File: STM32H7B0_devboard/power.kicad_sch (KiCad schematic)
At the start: 14 parts, among them Q4 AO3401A

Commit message: Breakout
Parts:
- C18: renamed from C26; footprint (none) -> NFM18PC104R1C3D:NFM18PC104R1C3D_MUR
- D3: renamed from D5; value 9v1 -> 10v; footprint (none) -> Diode_SMD:D_SOD-523
- renumbered C27 to C19, C28 to C20, C22 to C21, C29 to C22, C30 to C23, F3 to F1, L4 to L2, Q4 to Q2, R36 to R19, R34 to R20, R35 to R21, U7 to U4
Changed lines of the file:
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@@
 		(on_board yes)
 		(dnp no)
-		(property "Reference" "#PWR060"
+		(property "Reference" "#PWR043"
 			(at 93.98 95.25 0)
 			(effects
@@
 			(project "STM32H7B0_devboard"
 				(path "/0c02ba0f-c40f-484f-a270-dfb4a249f2e6/f5149cbb-8fa8-437a-8f6e-43d0a2b09eff"
-					(reference "#PWR060")
+					(reference "#PWR043")
 					(unit 1)
 				)
@@
 		(on_board yes)
 		(dnp no)
-		(property "Reference" "U7"
+		(property "Reference" "U4"
 			(at 115.57 26.67 0)
 			(effects
@@
 			)
 		)
-		(property "Datasheet" ""
+		(property "Datasheet" "https://www.lcsc.com/datasheet/lcsc_datasheet_2304241919_Texas-Instruments-TPS563201DDCR_C116592.pdf"
 			(at 110.49 33.02 0)
 			(effects
@@
 			(project "STM32H7B0_devboard"
 				(path "/0c02ba0f-c40f-484f-a270-dfb4a249f2e6/f5149cbb-8fa8-437a-8f6e-43d0a2b09eff"
-					(reference "U7")
+					(reference "U4")
 					(unit 1)
 				)
@@
 		(on_board yes)
 		(dnp no)
-		(property "Reference" "C28"
+		(property "Reference" "C20"
 			(at 87.122 32.512 0)
 			(effects
@@
 			(project "STM32H7B0_devboard"
 				(path "/0c02ba0f-c40f-484f-a270-dfb4a249f2e6/f5149cbb-8fa8-437a-8f6e-43d0a2b09eff"
-					(reference "C28")
+					(reference "C20")
 					(unit 1)
 				)
@@
 		(on_board yes)
 		(dnp no)
-		(property "Reference" "C29"
+		(property "Reference" "C22"
 			(at 71.882 80.772 0)
 			(effects
@@
 			(project "STM32H7B0_devboard"
 				(path "/0c02ba0f-c40f-484f-a270-dfb4a249f2e6/f5149cbb-8fa8-437a-8f6e-43d0a2b09eff"
-					(reference "C29")
+					(reference "C22")
 					(unit 1)
 				)
@@
 		(on_board yes)
 		(dnp no)
-		(property "Reference" "C27"
+		(property "Reference" "C19"
 			(at 80.772 32.512 0)
 			(effects
@@
 			(project "STM32H7B0_devboard"
 				(path "/0c02ba0f-c40f-484f-a270-dfb4a249f2e6/f5149cbb-8fa8-437a-8f6e-43d0a2b09eff"
-					(reference "C27")
+					(reference "C19")
 					(unit 1)
 				)
@@
 		(on_board yes)
 		(dnp no)
-		(property "Reference" "C26"
+		(property "Reference" "C18"
 			(at 72.39 26.67 0)
 			(effects
@@
 			)
 		)
-		(property "Footprint" ""
+		(property "Footprint" "NFM18PC104R1C3D:NFM18PC104R1C3D_MUR"
 			(at 72.39 31.75 90)
 			(effects
@@
 			)
 		)
-		(property "Datasheet" "~"
+		(property "Datasheet" "https://www.lcsc.com/datasheet/lcsc_datasheet_1811021520_Murata-Electronics-NFM18PC104R1C3D_C111493.pdf"
 			(at 72.39 31.75 90)
 			(effects
@@
 			)
 		)
-		(property "Description" "NFM31KC104R2A3L"
+		(property "Description" "NFM18PC104R1C3D"
 			(at 72.39 23.876 0)
 			(effects
@@
 					(size 1.27 1.27)
 				)
+				(hide yes)
 			)
 		)
@@
 			(project "STM32H7B0_devboard"
 				(path "/0c02ba0f-c40f-484f-a270-dfb4a249f2e6/f5149cbb-8fa8-437a-8f6e-43d0a2b09eff"
-					(reference "C26")
+					(reference "C18")
 					(unit 1)
 				)
@@
 		(on_board yes)
 		(dnp no)
-		(property "Reference" "#PWR062"
+		(property "Reference" "#PWR042"
 			(at 74.93 92.71 0)
 			(effects
@@
 			(project "STM32H7B0_devboard"
 				(path "/0c02ba0f-c40f-484f-a270-dfb4a249f2e6/f5149cbb-8fa8-437a-8f6e-43d0a2b09eff"
-					(reference "#PWR062")
+					(reference "#PWR042")
 					(unit 1)
 				)
@@
 		(on_board yes)
 		(dnp no)
-		(property "Reference" "R36"
+		(property "Reference" "R19"
 			(at 53.34 42.926 90)
 			(effects
@@
 			(project "STM32H7B0_devboard"
 				(path "/0c02ba0f-c40f-484f-a270-dfb4a249f2e6/f5149cbb-8fa8-437a-8f6e-43d0a2b09eff"
-					(reference "R36")
+					(reference "R19")
 					(unit 1)
 				)
@@
 		(on_board yes)
 		(dnp no)
-		(property "Reference" "#PWR061"
+		(property "Reference" "#PWR041"
 			(at 64.77 54.61 0)
 			(effects
@@
 			(project "STM32H7B0_devboard"
 				(path "/0c02ba0f-c40f-484f-a270-dfb4a249f2e6/f5149cbb-8fa8-437a-8f6e-43d0a2b09eff"
-					(reference "#PWR061")
+					(reference "#PWR041")
 					(unit 1)
 				)
@@
 		(on_board yes)
 		(dnp no)
-		(property "Reference" "R35"
+		(property "Reference" "R21"
 			(at 91.694 83.82 90)
 			(effects
@@
 			(project "STM32H7B0_devboard"
 				(path "/0c02ba0f-c40f-484f-a270-dfb4a249f2e6/f5149cbb-8fa8-437a-8f6e-43d0a2b09eff"
-					(reference "R35")
+					(reference "R21")
 					(unit 1)
 				)
@@
 		(on_board yes)
 		(dnp no)
-		(property "Reference" "F3"
+		(property "Reference" "F1"
 			(at 44.45 26.67 90)
 			(effects
@@
 			(project "STM32H7B0_devboard"
 				(path "/0c02ba0f-c40f-484f-a270-dfb4a249f2e6/f5149cbb-8fa8-437a-8f6e-43d0a2b09eff"
-					(reference "F3")
+					(reference "F1")
 					(unit 1)
 				)
@@
 		(on_board yes)
 		(dnp no)
-		(property "Reference" "C22"
+		(property "Reference" "C21"
 			(at 91.948 54.102 90)
 			(effects
@@
 			(project "STM32H7B0_devboard"
 				(path "/0c02ba0f-c40f-484f-a270-dfb4a249f2e6/f5149cbb-8fa8-437a-8f6e-43d0a2b09eff"
-					(reference "C22")
+					(reference "C21")
 					(unit 1)
 				)
@@
 		(on_board yes)
 		(dnp no)
-		(property "Reference" "L4"
+		(property "Reference" "L2"
 			(at 64.77 76.2 90)
 			(effects
@@
 			(project "STM32H7B0_devboard"
 				(path "/0c02ba0f-c40f-484f-a270-dfb4a249f2e6/f5149cbb-8fa8-437a-8f6e-43d0a2b09eff"
-					(reference "L4")
+					(reference "L2")
 					(unit 1)
 				)
@@
 		(on_board yes)
 		(dnp no)
-		(property "Reference" "C30"
+		(property "Reference" "C23"
 			(at 79.502 80.772 0)
 			(effects
@@
 			(project "STM32H7B0_devboard"
 				(path "/0c02ba0f-c40f-484f-a270-dfb4a249f2e6/f5149cbb-8fa8-437a-8f6e-43d0a2b09eff"
-					(reference "C30")
+					(reference "C23")
 					(unit 1)
 				)
@@
 		(on_board yes)
 		(dnp no)
-		(property "Reference" "#FLG07"
+		(property "Reference" "#FLG05"
 			(at 86.36 27.305 0)
 			(effects
@@
 			(project "STM32H7B0_devboard"
 				(path "/0c02ba0f-c40f-484f-a270-dfb4a249f2e6/f5149cbb-8fa8-437a-8f6e-43d0a2b09eff"
-					(reference "#FLG07")
+					(reference "#FLG05")
 					(unit 1)
 				)
@@
 		(on_board yes)
 		(dnp no)
-		(property "Reference" "#PWR051"
+		(property "Reference" "#PWR040"
 			(at 101.6 44.45 0)
 			(effects
@@
 			(project "STM32H7B0_devboard"
 				(path "/0c02ba0f-c40f-484f-a270-dfb4a249f2e6/f5149cbb-8fa8-437a-8f6e-43d0a2b09eff"
-					(reference "#PWR051")
+					(reference "#PWR040")
 					(unit 1)
 				)
@@
 		(on_board yes)
 		(dnp no)
-		(property "Reference" "R34"
+		(property "Reference" "R20"
 			(at 89.154 76.2 90)
 			(effects
@@
 			(project "STM32H7B0_devboard"
 				(path "/0c02ba0f-c40f-484f-a270-dfb4a249f2e6/f5149cbb-8fa8-437a-8f6e-43d0a2b09eff"
-					(reference "R34")
+					(reference "R20")
 					(unit 1)
 				)
@@
 		(on_board yes)
 		(dnp no)
-		(property "Reference" "D5"
+		(property "Reference" "D3"
 			(at 61.214 31.496 0)
 			(effects
@@
 			)
 		)
-		(property "Value" "9v1"
+		(property "Value" "10v"
 			(at 66.04 31.242 0)
 			(effects
@@
 			)
 		)
-		(property "Footprint" ""
+		(property "Footprint" "Diode_SMD:D_SOD-523"
 			(at 63.5 33.02 90)
 			(effects
@@
 			)
 		)
-		(property "Datasheet" "~"
+		(property "Datasheet" "https://www.lcsc.com/datasheet/lcsc_datasheet_2304140030_Nexperia-BZX585-B10-115_C455021.pdf"
 			(at 63.5 33.02 90)
 			(effects
@@
 			)
 		)
-		(property "Description" "BZX585-B9v1"
+		(property "Description" "BZX585-B10"
 			(at 63.5 21.082 90)
 			(effects
@@
 					(size 1.27 1.27)
 				)
-			)
-		)
-		(pin "2"
-		)
-		(pin "1"
-		)
-		(instances
-			(project "STM32H7B0_devboard"
-				(path "/0c02ba0f-c40f-484f-a270-dfb4a249f2e6/f5149cbb-8fa8-437a-8f6e-43d0a2b09eff"
-					(reference "D5")
+				(hide yes)
+			)
+		)
+		(pin "2"
+		)
+		(pin "1"
+		)
+		(instances
+			(project "STM32H7B0_devboard"
+				(path "/0c02ba0f-c40f-484f-a270-dfb4a249f2e6/f5149cbb-8fa8-437a-8f6e-43d0a2b09eff"
+					(reference "D3")
 					(unit 1)
 				)
@@
 		(on_board yes)
 		(dnp no)
-		(property "Reference" "Q4"
+		(property "Reference" "Q2"
 			(at 55.88 25.654 90)
 			(effects
@@
 					(size 1.27 1.27)
 				)
+				(hide yes)
 			)
 		)
@@
 			(project "STM32H7B0_devboard"
 				(path "/0c02ba0f-c40f-484f-a270-dfb4a249f2e6/f5149cbb-8fa8-437a-8f6e-43d0a2b09eff"
-					(reference "Q4")
-					(unit 1)
-				)
+					(reference "Q2")
+					(unit 1)
+				)

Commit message: Schematic V2.0 + Footprints
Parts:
- L2: footprint (none) -> Inductor_SMD:L_0603_1608Metric
- R19, R20, R21: footprint (none) -> Resistor_SMD:R_0402_1005Metric
- U4: footprint (none) -> Package_TO_SOT_SMD:SOT-23-6
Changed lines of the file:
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@@
 			)
 		)
-		(property "Footprint" ""
+		(property "Footprint" "Package_TO_SOT_SMD:SOT-23-6"
 			(at 110.49 33.02 0)
 			(effects
@@
 			)
 		)
-		(property "Footprint" ""
+		(property "Footprint" "Resistor_SMD:R_0402_1005Metric"
 			(at 55.88 43.18 0)
 			(effects
@@
 			)
 		)
-		(property "Footprint" ""
+		(property "Footprint" "Resistor_SMD:R_0402_1005Metric"
 			(at 93.98 83.82 0)
 			(effects
@@
 			)
 		)
-		(property "Footprint" ""
+		(property "Footprint" "Inductor_SMD:L_0603_1608Metric"
 			(at 64.77 78.74 0)
 			(effects
@@
 			)
 		)
-		(property "Description" "Inductor, small symbol"
+		(property "Description" "MPL1608S2R2MHT"
 			(at 64.77 78.74 0)
 			(effects
@@
 			)
 		)
-		(property "Footprint" ""
+		(property "Footprint" "Resistor_SMD:R_0402_1005Metric"
 			(at 88.9 78.74 0)
 			(effects

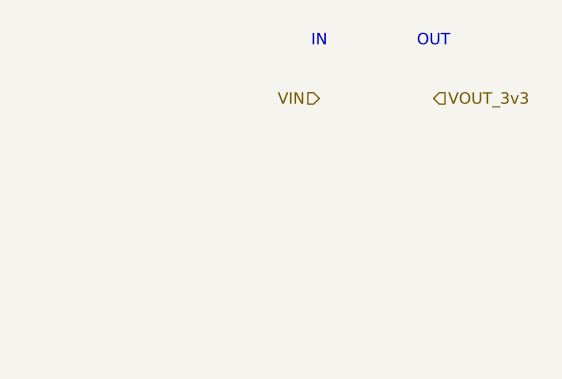
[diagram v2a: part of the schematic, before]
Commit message: Updated .gitignore
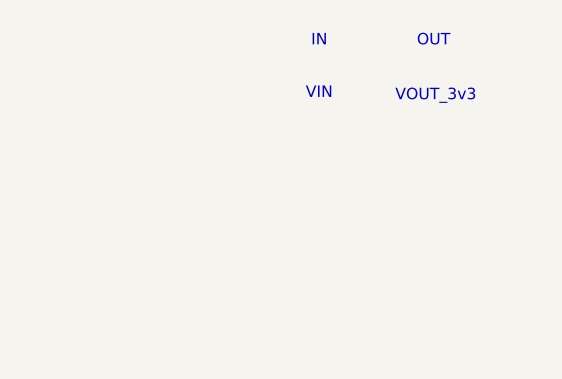
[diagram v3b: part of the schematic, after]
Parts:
- C21: footprint Capacitor_SMD:C_0603_1608Metric -> Capacitor_SMD:C_1206_3216Metric
- L2: footprint Inductor_SMD:L_0603_1608Metric -> Inductor_SMD:L_Changjiang_FNR3015S
- R19, R20, R21: footprint Resistor_SMD:R_0402_1005Metric -> Resistor_SMD:R_0603_1608Metric
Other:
- note added: "VIN"
- note added: "VOUT_3v3"
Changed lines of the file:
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@@
+		)
+	)
+	(text "VOUT_3v3"
+		(exclude_from_sim no)
+		(at 260.604 25.146 0)
+		(effects
+			(font
+				(size 1.27 1.27)
+			)
 		)
 	)
@@
 		(exclude_from_sim no)
 		(at 247.65 19.05 0)
+		(effects
+			(font
+				(size 1.27 1.27)
+			)
+		)
+	)
+	(text "VIN"
+		(exclude_from_sim no)
+		(at 247.65 24.892 0)
 		(effects
 			(font
@@
 		)
 	)
+	(label "BUCK_SW"
+		(at 102.87 34.29 180)
+		(fields_autoplaced yes)
+		(effects
+			(font
+				(size 1.27 1.27)
+			)
+			(justify right bottom)
+		)
+	)
+	(label "BUCK_FB"
+		(at 97.79 80.01 0)
+		(fields_autoplaced yes)
+		(effects
+			(font
+				(size 1.27 1.27)
+			)
+			(justify left bottom)
+		)
+	)
+	(label "BUCK_EN"
+		(at 91.44 29.21 0)
+		(fields_autoplaced yes)
+		(effects
+			(font
+				(size 1.27 1.27)
+			)
+			(justify left bottom)
+		)
+	)
 	(label "BUCK_EN"
 		(at 119.38 34.29 0)
@@
 			(justify left bottom)
 		)
-		(property "Netclass" ""
-			(at 119.38 35.56 0)
-			(effects
-				(font
-					(size 1.27 1.27)
-				)
-				(justify left)
-				(hide yes)
-			)
-		)
-	)
-	(label "BUCK_SW"
-		(at 102.87 34.29 180)
-		(fields_autoplaced yes)
-		(effects
-			(font
-				(size 1.27 1.27)
-			)
-			(justify right bottom)
-		)
-	)
-	(label "BUCK_FB"
-		(at 97.79 80.01 0)
-		(fields_autoplaced yes)
-		(effects
-			(font
-				(size 1.27 1.27)
-			)
-			(justify left bottom)
-		)
-	)
-	(label "BUCK_EN"
-		(at 91.44 29.21 0)
-		(fields_autoplaced yes)
-		(effects
-			(font
-				(size 1.27 1.27)
-			)
-			(justify left bottom)
-		)
 	)
 	(label "BUCK_BST"
@@
 			)
 			(justify left bottom)
-		)
-	)
-	(hierarchical_label "VOUT_3v3"
-		(shape input)
-		(at 260.35 25.4 0)
-		(fields_autoplaced yes)
-		(effects
-			(font
-				(size 1.27 1.27)
-			)
-			(justify left)
 		)
 	)
@@
 		)
 	)
-	(hierarchical_label "VIN"
-		(shape input)
-		(at 247.65 25.4 180)
-		(fields_autoplaced yes)
-		(effects
-			(font
-				(size 1.27 1.27)
-			)
-			(justify right)
-		)
-	)
 	(hierarchical_label "VOUT_3v3"
 		(shape input)
@@
 			)
 		)
-		(property "Footprint" "Resistor_SMD:R_0402_1005Metric"
+		(property "Footprint" "Resistor_SMD:R_0603_1608Metric"
 			(at 55.88 43.18 0)
 			(effects
@@
 			)
 		)
-		(property "Footprint" "Resistor_SMD:R_0402_1005Metric"
+		(property "Footprint" "Resistor_SMD:R_0603_1608Metric"
 			(at 93.98 83.82 0)
 			(effects
@@
 			)
 		)
-		(property "Footprint" "Capacitor_SMD:C_0603_1608Metric"
+		(property "Footprint" "Capacitor_SMD:C_1206_3216Metric"
 			(at 90.17 57.15 0)
 			(effects
@@
 			)
 		)
-		(property "Footprint" "Inductor_SMD:L_0603_1608Metric"
+		(property "Footprint" "Inductor_SMD:L_Changjiang_FNR3015S"
 			(at 64.77 78.74 0)
 			(effects
@@
 			)
 		)
-		(property "Description" "MPL1608S2R2MHT"
+		(property "Description" "FNR3015S2R2MT"
 			(at 64.77 78.74 0)
 			(effects
@@
 			)
 		)
-		(property "Footprint" "Resistor_SMD:R_0402_1005Metric"
+		(property "Footprint" "Resistor_SMD:R_0603_1608Metric"
 			(at 88.9 78.74 0)
 			(effects

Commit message: Done V1
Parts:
- C18: LCSC (none) -> C111493
- C19, C20: LCSC (none) -> C9807
- C21: LCSC (none) -> C110255
- C22, C23: LCSC (none) -> C12891
- D3: LCSC (none) -> C455021
- F1: LCSC (none) -> C2830236
- L2: LCSC (none) -> C167747
- Q2: LCSC (none) -> C347476
- R19, R21: LCSC (none) -> C25804
- R20: LCSC (none) -> C23003
- U4: LCSC (none) -> C116592
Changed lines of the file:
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@@
+			)
+		)
+		(property "LCSC" "C116592"
+			(at 110.49 33.02 0)
+			(effects
+				(font
+					(size 1.27 1.27)
+				)
+				(hide yes)
 			)
 		)
@@
 			)
 		)
+		(property "LCSC" " C9807"
+			(at 86.36 34.29 0)
+			(effects
+				(font
+					(size 1.27 1.27)
+				)
+				(hide yes)
+			)
+		)
 		(pin "2"
 		)
@@
 			)
 		)
+		(property "LCSC" "C12891"
+			(at 71.12 82.55 0)
+			(effects
+				(font
+					(size 1.27 1.27)
+				)
+				(hide yes)
+			)
+		)
 		(pin "2"
 		)
@@
 			)
 		)
+		(property "LCSC" " C9807"
+			(at 80.01 34.29 0)
+			(effects
+				(font
+					(size 1.27 1.27)
+				)
+				(hide yes)
+			)
+		)
 		(pin "2"
 		)
@@
 			)
 		)
+		(property "LCSC" "C111493"
+			(at 72.39 31.75 0)
+			(effects
+				(font
+					(size 1.27 1.27)
+				)
+				(hide yes)
+			)
+		)
 		(pin "1"
 		)
@@
 			)
 		)
+		(property "LCSC" "C25804"
+			(at 55.88 43.18 0)
+			(effects
+				(font
+					(size 1.27 1.27)
+				)
+				(hide yes)
+			)
+		)
 		(pin "1"
 		)
@@
 			)
 		)
+		(property "LCSC" "C25804"
+			(at 93.98 83.82 0)
+			(effects
+				(font
+					(size 1.27 1.27)
+				)
+				(hide yes)
+			)
+		)
 		(pin "1"
 		)
@@
 			)
 		)
+		(property "LCSC" "C2830236"
+			(at 44.45 29.21 0)
+			(effects
+				(font
+					(size 1.27 1.27)
+				)
+				(hide yes)
+			)
+		)
 		(pin "2"
 		)
@@
 			)
 		)
+		(property "LCSC" "C110255"
+			(at 90.17 57.15 0)
+			(effects
+				(font
+					(size 1.27 1.27)
+				)
+				(hide yes)
+			)
+		)
 		(pin "2"
 		)
@@
 			)
 		)
+		(property "LCSC" "C167747"
+			(at 64.77 78.74 0)
+			(effects
+				(font
+					(size 1.27 1.27)
+				)
+				(hide yes)
+			)
+		)
 		(pin "2"
 		)
@@
 			)
 		)
+		(property "LCSC" "C12891"
+			(at 78.74 82.55 0)
+			(effects
+				(font
+					(size 1.27 1.27)
+				)
+				(hide yes)
+			)
+		)
 		(pin "2"
 		)
@@
 			)
 		)
+		(property "LCSC" " C23003"
+			(at 88.9 78.74 0)
+			(effects
+				(font
+					(size 1.27 1.27)
+				)
+				(hide yes)
+			)
+		)
 		(pin "1"
 		)
@@
 			)
 		)
+		(property "LCSC" "C455021"
+			(at 63.5 33.02 0)
+			(effects
+				(font
+					(size 1.27 1.27)
+				)
+				(hide yes)
+			)
+		)
 		(pin "2"
 		)
@@
 			(effects
 				(font
+					(size 1.27 1.27)
+				)
+				(hide yes)
+			)
+		)
+		(property "LCSC" "C347476"
+			(at 55.88 31.75 0)
+			(effects
+				(font

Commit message: Finished board
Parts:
- C19, C20: LCSC C9807 -> C13585
- C21: LCSC C110255 -> C24497
- Q2: LCSC C347476 -> C15127
- R20: LCSC C23003 -> C23003
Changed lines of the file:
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@@
 			)
 		)
-		(property "LCSC" " C9807"
+		(property "LCSC" " C13585"
 			(at 86.36 34.29 0)
 			(effects
@@
 			)
 		)
-		(property "LCSC" " C9807"
+		(property "LCSC" " C13585"
 			(at 80.01 34.29 0)
 			(effects
@@
 			)
 		)
-		(property "LCSC" "C110255"
+		(property "LCSC" "C24497"
 			(at 90.17 57.15 0)
 			(effects
@@
 			)
 		)
-		(property "LCSC" " C23003"
+		(property "LCSC" "C23003"
 			(at 88.9 78.74 0)
 			(effects
@@
 			)
 		)
-		(property "LCSC" "C347476"
+		(property "LCSC" "C15127"
 			(at 55.88 31.75 0)
 			(effects
